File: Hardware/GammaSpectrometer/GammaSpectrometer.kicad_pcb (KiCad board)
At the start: 2 copper layers, 98 x 86 mm, 59 parts, among them J1 power supply, J2 anode, J3 cathode, J4 Conn_01x07_Female, J5 RF_Shield_Two_Pieces, Q1 AOD2810, U1 MCP1416

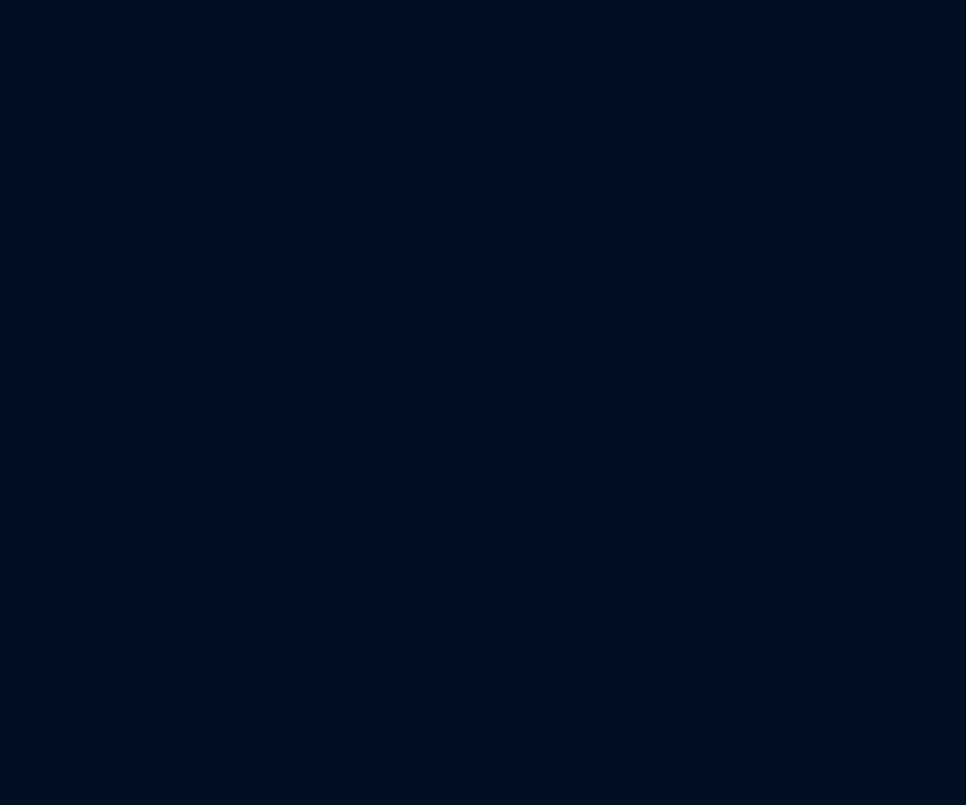
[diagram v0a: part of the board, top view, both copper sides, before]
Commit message: HV Power Supply and DataAcquisition will be placed on the same PCB. Due to EMI it mightl be needed to mount them on separate PCB, still they will share the same layout. This will decrease amount of needed PCBs and reduce costs.
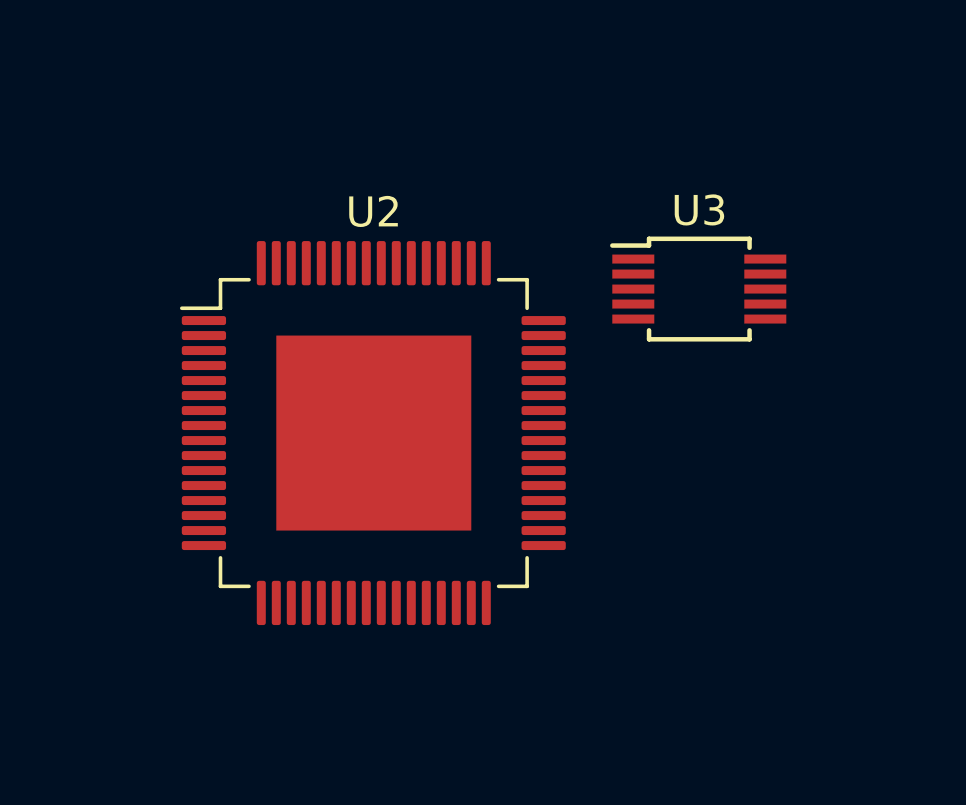
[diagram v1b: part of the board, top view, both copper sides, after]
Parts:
- added U2: PIC32MZ0512EFE064, Package_QFP:LQFP-64-1EP_10x10mm_P0.5mm_EP6.5x6.5mm, F.Cu at (82.8, 106.7)
- added U3: MCP33131-10, Package_SO:MSOP-10_3x3mm_P0.5mm, F.Cu at (93.7, 101.9)
- J1: footprint HighVoltagePowerSupply:DG300-5.0-02P-12-00A(H) -> GammaSpectrometer:DG300-5.0-02P-12-00A(H)
- J5: footprint HighVoltagePowerSupply:3710.16 -> GammaSpectrometer:3710.16
- TR1: footprint HighVoltagePowerSupply:RM8 -> GammaSpectrometer:RM8
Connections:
- net /V_DIVIDER renamed /HighVoltagePowerSupply/V_DIVIDER

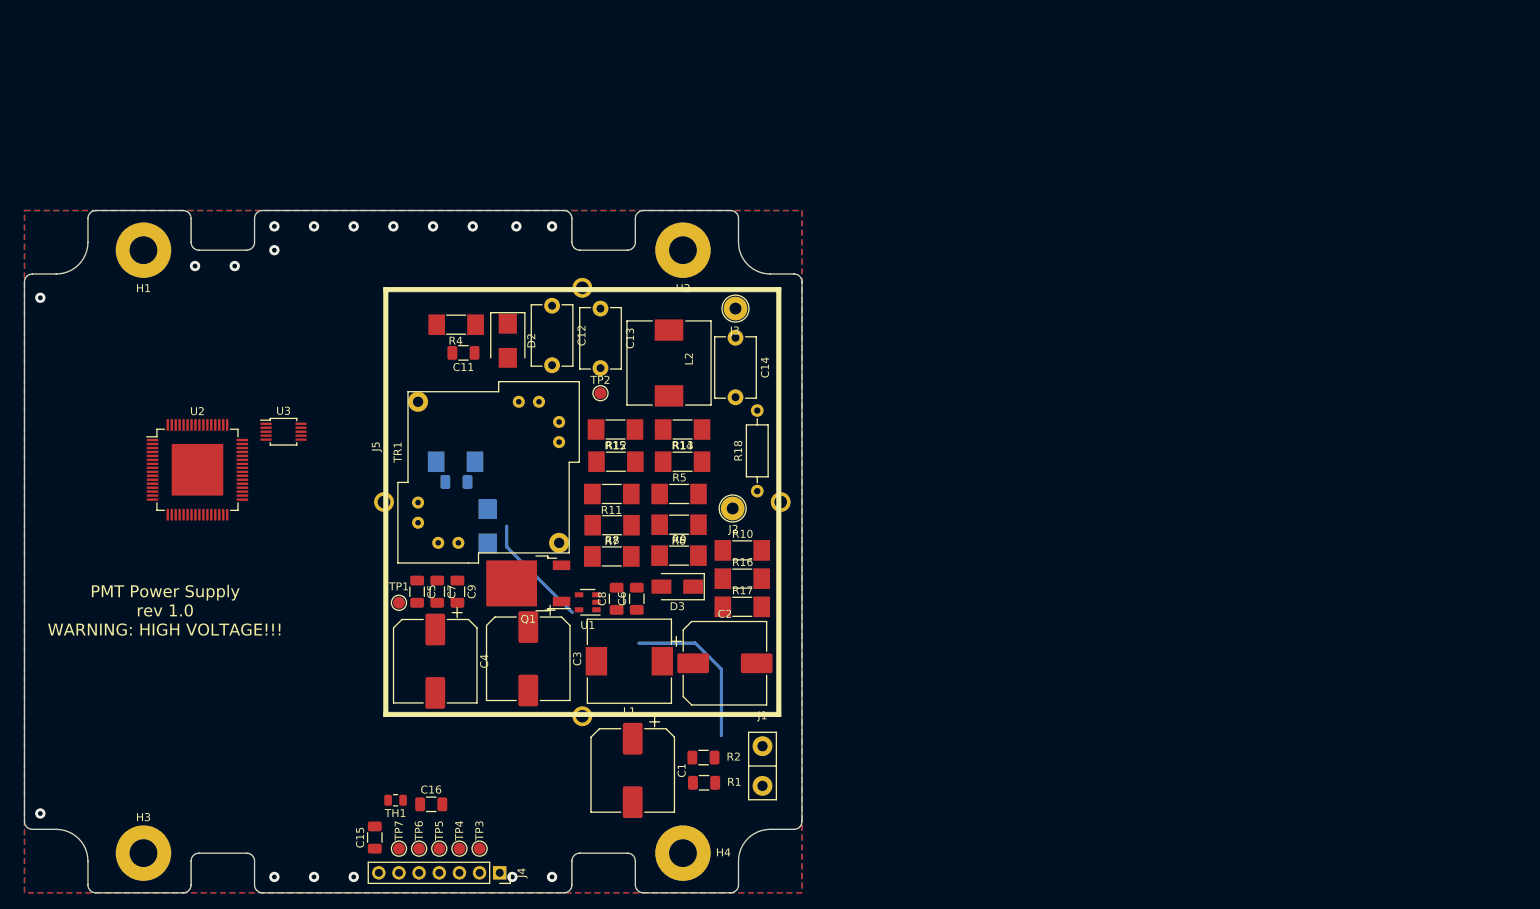
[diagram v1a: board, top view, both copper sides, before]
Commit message: draft of component placement on PCB
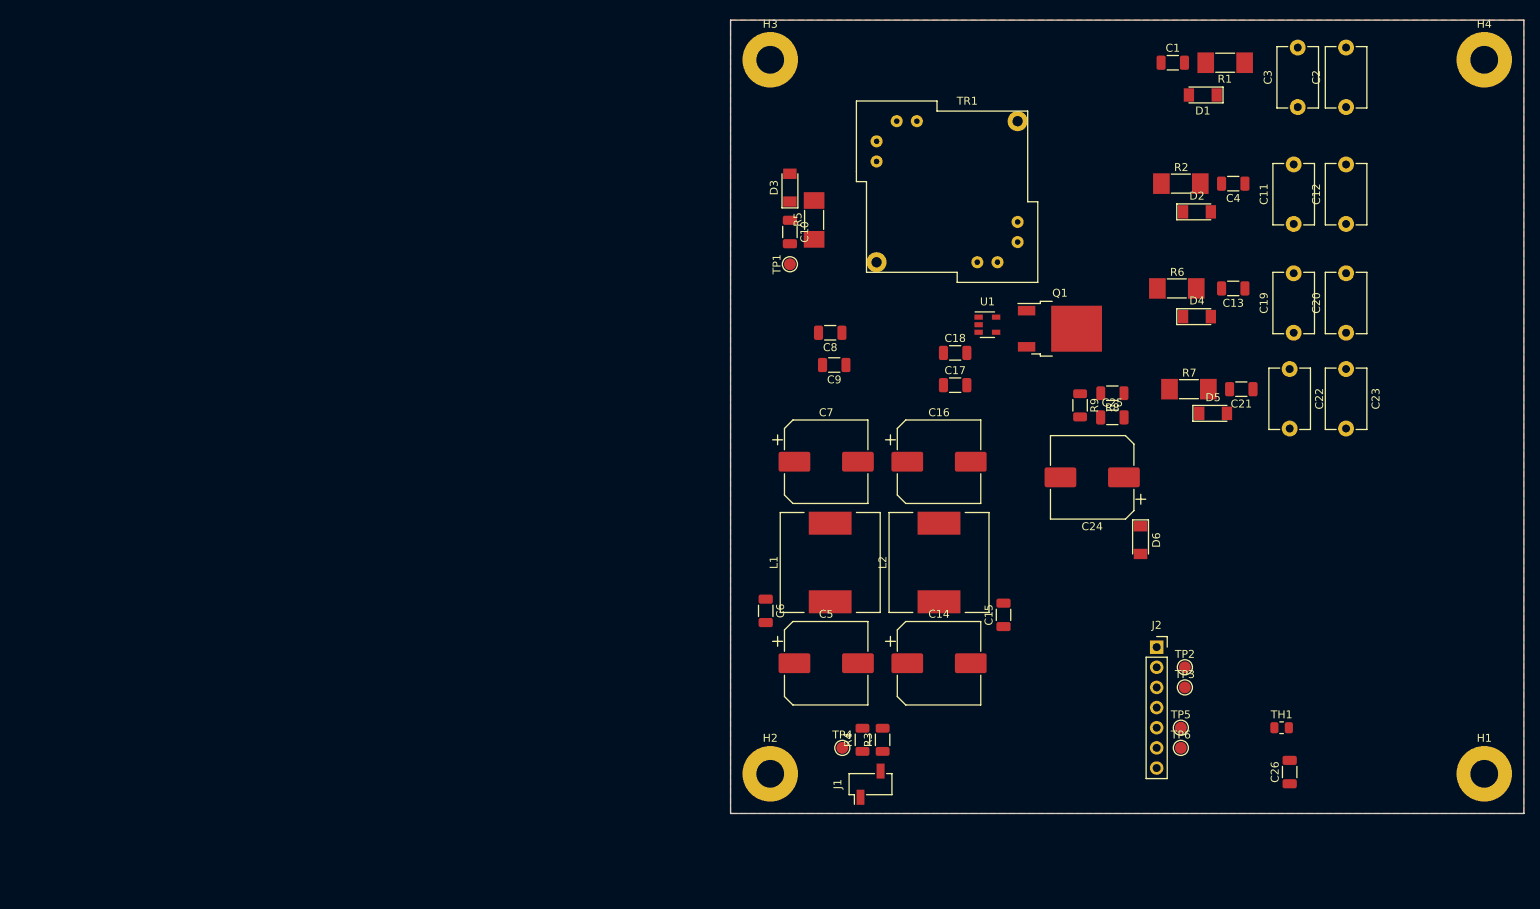
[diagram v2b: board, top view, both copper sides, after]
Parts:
- removed J3: cathode, TestPoint:TestPoint_Loop_D2.54mm_Drill1.5mm_Beaded
- removed J4: Conn_01x07_Female, Connector_PinSocket_2.54mm:PinSocket_1x07_P2.54mm_Vertical
- removed J5: RF_Shield_Two_Pieces, GammaSpectrometer:3710.16
- removed R10: 5k6, Resistor_SMD:R_MELF_MMB-0207
- removed R11, R12, R13, R14, R15: 10M, Resistor_SMD:R_MELF_MMB-0207
- removed R16, R17: 47k, Resistor_SMD:R_MELF_MMB-0207
- removed R18: TBD, Resistor_THT:R_Axial_DIN0207_L6.3mm_D2.5mm_P10.16mm_Horizontal
- removed TP7: TEMP_MONITOR, TestPoint:TestPoint_Pad_D1.5mm
- removed U2: PIC32MZ0512EFE064, Package_QFP:LQFP-64-1EP_10x10mm_P0.5mm_EP6.5x6.5mm
- removed U3: MCP33131-10, Package_SO:MSOP-10_3x3mm_P0.5mm
- added C17: 100n, Capacitor_SMD:C_1206_3216Metric, F.Cu at (178.3, 96.0)
- added C18: 100n, Capacitor_SMD:C_1206_3216Metric, F.Cu at (178.3, 91.9)
- added C19: 10n/2kV, Capacitor_THT:C_Disc_D7.5mm_W5.0mm_P7.50mm, F.Cu at (221.0, 89.4)
- added C20: 10n/2kV, Capacitor_THT:C_Disc_D7.5mm_W5.0mm_P7.50mm, F.Cu at (227.6, 89.4)
- added C21: TBD, Capacitor_SMD:C_1206_3216Metric, F.Cu at (214.4, 96.5)
- added C22: 10n/2kV, Capacitor_THT:C_Disc_D7.5mm_W5.0mm_P7.50mm, F.Cu at (220.5, 94.0)
- added C23: 10n/2kV, Capacitor_THT:C_Disc_D7.5mm_W5.0mm_P7.50mm, F.Cu at (227.6, 94.0)
- added C24: 10u/12V, Capacitor_SMD:CP_Elec_10x10, F.Cu at (195.6, 107.6)
- added C25: 100n, Capacitor_SMD:C_1206_3216Metric, F.Cu at (198.1, 100.1)
- added C26: 1n, Capacitor_SMD:C_1206_3216Metric, F.Cu at (220.5, 144.8)
- added D4: HER208, Diode_SMD:D_MiniMELF, F.Cu at (208.8, 87.4)
- added D5: HER208, Diode_SMD:D_MiniMELF, F.Cu at (210.8, 99.6)
- added D6: D, Diode_SMD:D_MiniMELF, F.Cu at (201.7, 115.5)
- C1, C4: value 470u/25V -> TBD; footprint Capacitor_SMD:CP_Elec_10x10 -> Capacitor_SMD:C_1206_3216Metric
- C10: moved to F.Cu
- C11: value TBD -> 10n/2kV; footprint Capacitor_SMD:C_1206_3216Metric -> Capacitor_THT:C_Disc_D7.5mm_W5.0mm_P7.50mm
- C13: value 10n/2kV -> TBD; footprint Capacitor_THT:C_Disc_D7.5mm_W5.0mm_P7.50mm -> Capacitor_SMD:C_1206_3216Metric
- C14: value 10n/2kV -> 470u/25V; footprint Capacitor_THT:C_Disc_D7.5mm_W5.0mm_P7.50mm -> Capacitor_SMD:CP_Elec_10x10
- C15: value 1n -> 1u
- C16: value 1n -> 470u/25V; footprint Capacitor_SMD:C_1206_3216Metric -> Capacitor_SMD:CP_Elec_10x10
- C2, C3: value 470u/25V -> 10n/2kV; footprint Capacitor_SMD:CP_Elec_10x10 -> Capacitor_THT:C_Disc_D7.5mm_W5.0mm_P7.50mm
- C5, C7: value 10u -> 470u/25V; footprint Capacitor_SMD:C_1206_3216Metric -> Capacitor_SMD:CP_Elec_10x10
- C6: value 1u -> 10u
- C8: value 100n -> 10u
- D1: value TBD -> HER208; footprint Diode_SMD:D_SMB -> Diode_SMD:D_MiniMELF; moved to F.Cu
- D2: value SM518 -> HER208; footprint Diode_SMD:D_SMB -> Diode_SMD:D_MiniMELF
- D3: value 5V -> TBD; footprint Diode_SMD:D_SMA -> Diode_SMD:D_MiniMELF
- J1: footprint GammaSpectrometer:DG300-5.0-02P-12-00A(H) -> Connector_PinSocket_2.54mm:PinSocket_1x02_P2.54mm_Vertical_SMD_Pin1Left
- J2: value anode -> Conn_01x07_Female; footprint TestPoint:TestPoint_Loop_D2.54mm_Drill1.5mm_Beaded -> Connector_PinSocket_2.54mm:PinSocket_1x07_P2.54mm_Vertical
- L1: footprint Inductor_SMD:L_10.4x10.4_H4.8 -> Inductor_SMD:L_12x12mm_H6mm
- L2: value L -> TBD; footprint Inductor_SMD:L_10.4x10.4_H4.8 -> Inductor_SMD:L_12x12mm_H6mm
- R1, R2: value 1R -> TBD; footprint Resistor_SMD:R_1206_3216Metric -> Resistor_SMD:R_MELF_MMB-0207
- R3: value TBD -> 1R; footprint Resistor_SMD:R_MELF_MMB-0207 -> Resistor_SMD:R_1206_3216Metric; moved to F.Cu
- R4: value TBD -> 1R; footprint Resistor_SMD:R_MELF_MMB-0207 -> Resistor_SMD:R_1206_3216Metric
- R5, R6, R7: value 10M -> TBD
- R8, R9: value 10M -> 6k8; footprint Resistor_SMD:R_MELF_MMB-0207 -> Resistor_SMD:R_1206_3216Metric
- TP2: value TestPoint -> HV_MONITOR
- TP3: value HV_MONITOR -> ENABLE
- TP4: value ENABLE -> IN_CURRENT_MONITOR_1
- TP5: value IN_CURRENT_MONITOR_1 -> IN_CURRENT_MONITOR_2
- TP6: value IN_CURRENT_MONITOR_2 -> TEMP_MONITOR
- moved H1 181.4 mm to (245.0, 145.0)
- moved H4 142.1 mm to (245.0, 55.0)
- moved H3 127.4 mm to (155.0, 55.0)
- moved C3 119.3 mm to (221.5, 61.0), turned to 90 degrees
- moved C4 117.2 mm to (213.4, 70.6), turned to 180 degrees
- moved C1 112.2 mm to (205.7, 55.4), turned to 0 degrees
- moved TH1 112.1 mm to (219.5, 139.2), turned to 0 degrees
- moved R1 112.0 mm to (212.3, 55.4)
- moved C11 105.9 mm to (221.0, 75.7), turned to 90 degrees
- moved D1 105.3 mm to (209.5, 59.4), turned to 180 degrees
- moved C2 105.1 mm to (227.6, 61.0), turned to 90 degrees
- moved C12 100.6 mm to (227.6, 75.7), turned to 90 degrees
- moved TP6 96.8 mm to (206.8, 141.7)
- moved TP5 94.7 mm to (206.8, 139.2)
- moved R2 94.1 mm to (206.8, 70.6), turned to 0 degrees
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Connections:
- C1 pad 2: GND -> Net-(C1-Pad2)
- C12 pad 1: GND -> Net-(C11-Pad1)
- C12 pad 2: Net-(C12-Pad2) -> Net-(C11-Pad2)
- C13 pad 1: GND -> Net-(C13-Pad1)
- C13 pad 2: Net-(C12-Pad2) -> Net-(C13-Pad2)
- C14 pad 1: GND -> /HighVoltagePowerSupply/IN_CURRENT_MONITOR_2
- C14 pad 2: Net-(C14-Pad2) -> GND
- C15 pad 2: /HighVoltagePowerSupply/V_DIVIDER -> /HighVoltagePowerSupply/IN_CURRENT_MONITOR_2
- C16 pad 1: GND -> Net-(C16-Pad1)
- C16 pad 2: Net-(C16-Pad2) -> GND
- C2 pad 1: Net-(C1-Pad1) -> Net-(C11-Pad2)
- C2 pad 2: GND -> HV+
- C3 pad 1: Net-(C10-Pad2) -> Net-(C11-Pad2)
- C3 pad 2: GND -> HV+
- C4 pad 1: Net-(C10-Pad2) -> Net-(C4-Pad1)
- C4 pad 2: GND -> Net-(C4-Pad2)
- C5 pad 1: GND -> /HighVoltagePowerSupply/IN_CURRENT_MONITOR_2
- C5 pad 2: Net-(C10-Pad2) -> GND
- C6 pad 2: Net-(C1-Pad1) -> /HighVoltagePowerSupply/IN_CURRENT_MONITOR_2
- C7 pad 1: GND -> Net-(C10-Pad2)
- C7 pad 2: Net-(C10-Pad2) -> GND
- C8 pad 2: Net-(C1-Pad1) -> Net-(C10-Pad2)
- D1 pad 1: Net-(C10-Pad1) -> HV+
- D1 pad 2: Net-(D1-Pad2) -> Net-(C1-Pad1)
- D2 pad 1: Net-(C12-Pad2) -> Net-(C11-Pad2)
- D2 pad 2: Net-(C11-Pad1) -> Net-(C4-Pad1)
- D3 pad 1: /HighVoltagePowerSupply/V_DIVIDER -> Net-(C10-Pad1)
- D3 pad 2: GND -> Net-(D3-Pad2)
- J1 pad 1: Net-(J1-Pad1) -> /HighVoltagePowerSupply/IN_CURRENT_MONITOR_1
- J2 pad 1: Net-(J2-Pad1) -> (no net)
- L1 pad 1: Net-(C1-Pad1) -> /HighVoltagePowerSupply/IN_CURRENT_MONITOR_2
- L2 pad 1: Net-(C12-Pad2) -> /HighVoltagePowerSupply/IN_CURRENT_MONITOR_2
- L2 pad 2: Net-(C14-Pad2) -> Net-(C16-Pad1)
- Q1 pad 2: Net-(D1-Pad2) -> Net-(D3-Pad2)
- R1 pad 1: Net-(J1-Pad1) -> HV+
- R1 pad 2: Net-(C1-Pad1) -> Net-(C1-Pad2)
- R2 pad 1: Net-(J1-Pad1) -> Net-(C11-Pad2)
- R2 pad 2: Net-(C1-Pad1) -> Net-(C4-Pad2)
- R3 pad 1: Net-(C10-Pad2) -> /HighVoltagePowerSupply/IN_CURRENT_MONITOR_1
- R3 pad 2: Net-(C10-Pad1) -> /HighVoltagePowerSupply/IN_CURRENT_MONITOR_2
- R4 pad 1: Net-(C12-Pad2) -> /HighVoltagePowerSupply/IN_CURRENT_MONITOR_1
- R4 pad 2: Net-(C11-Pad2) -> /HighVoltagePowerSupply/IN_CURRENT_MONITOR_2
- R5 pad 1: Net-(R11-Pad1) -> Net-(C10-Pad2)
- R5 pad 2: Net-(R5-Pad2) -> Net-(C10-Pad1)
- R6 pad 1: Net-(R5-Pad2) -> Net-(C11-Pad1)
- R6 pad 2: Net-(R6-Pad2) -> Net-(C13-Pad2)
- R7 pad 1: Net-(R6-Pad2) -> HV_REG+
- R7 pad 2: Net-(R7-Pad2) -> Net-(C21-Pad2)
- R8 pad 1: Net-(R7-Pad2) -> Net-(C24-Pad1)
- R8 pad 2: Net-(R8-Pad2) -> /HighVoltagePowerSupply/HV_MONITOR
- R9 pad 1: Net-(R8-Pad2) -> /HighVoltagePowerSupply/HV_MONITOR
- R9 pad 2: /HighVoltagePowerSupply/V_DIVIDER -> GND
- TH1 pad 1: Net-(C16-Pad2) -> Net-(C26-Pad2)
- TP2 pad 1: Net-(C12-Pad2) -> /HighVoltagePowerSupply/HV_MONITOR
- TP3 pad 1: Net-(J4-Pad2) -> /HighVoltagePowerSupply/ENABLE
- TP4 pad 1: Net-(J4-Pad3) -> /HighVoltagePowerSupply/IN_CURRENT_MONITOR_1
- TP5 pad 1: Net-(J1-Pad1) -> /HighVoltagePowerSupply/IN_CURRENT_MONITOR_2
- TP6 pad 1: Net-(C1-Pad1) -> Net-(C26-Pad2)
- TR1 pad 1: (no net) -> Net-(C11-Pad1)
- TR1 pad 11: Net-(D1-Pad2) -> Net-(C11-Pad2)
- TR1 pad 12: (no net) -> Net-(C1-Pad1)
- TR1 pad 2: Net-(C10-Pad2) -> Net-(C13-Pad1)
- TR1 pad 5: Net-(C11-Pad1) -> Net-(C10-Pad2)
- TR1 pad 6: (no net) -> Net-(D3-Pad2)
- TR1 pad 7: (no net) -> Net-(D6-Pad2)
- U1 pad 2: Net-(C1-Pad1) -> Net-(C16-Pad1)
- U1 pad 3: Net-(J4-Pad3) -> /HighVoltagePowerSupply/ENABLE
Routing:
- net Net-(J1-Pad1): track 20.1 -> 0.00 mm
- net /VCC_OPAMP: track 14.3 -> 0.00 mm
- net GND: vias 18 -> 0
- removed copper zone on B.Cu, net GND
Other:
- board size 98 x 86 mm -> 100 x 100 mm
- board text removed: "PMT Power Supply rev 1.0 WARNING: HIGH VOLTAGE!!!"

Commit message: switch to kicad6, version before moving to in serries 400v stabilizers
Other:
- net class Default removed
- net class high voltage removed
